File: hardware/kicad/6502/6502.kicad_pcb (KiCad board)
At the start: 2 copper layers, 35 parts, among them J1 Barrel_Jack, J2 Bus_Header, J3 VIA_Header, SW1 SW_Push, SW2 SW_Push, SW3 SW_Push, SW4 SW_Push, SW5 SW_Push, U1 L7805, U2 W65C02SxP, U3 28C256, U4 HM62256BLP, U5 W65C22SxP, U6 74LS00, U7 74LS00, X1 CXO_DIP8, X1 TFT680

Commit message: End of day 8/24.
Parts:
- removed the X1 at (179.1, 90.2)
- added G***: LOGO, Graphics:logo, F.Cu at (196.0, 119.0)
- added REF**: MountingHole_3.5mm, MountingHole:MountingHole_3.5mm, F.Cu at (63.5, 143.5)
- added REF**: MountingHole_3.5mm, MountingHole:MountingHole_3.5mm, F.Cu at (223.5, 143.5)
- added REF**: MountingHole_3.5mm, MountingHole:MountingHole_3.5mm, F.Cu at (63.0, 36.5)
- added REF**: MountingHole_3.5mm, MountingHole:MountingHole_3.5mm, F.Cu at (223.0, 37.5)
- R1, R2, R3, R4, R5, R6: footprint Resistor_THT:R_Axial_Power_L25.0mm_W9.0mm_P10.16mm_Vertical -> Resistor_THT:R_Axial_DIN0207_L6.3mm_D2.5mm_P10.16mm_Horizontal
- U1: footprint Package_TO_SOT_THT:TO-220-5_Horizontal_TabDown -> Package_TO_SOT_THT:TO-220-3_Horizontal_TabDown
- U3, U4: footprint Package_DIP:DIP-28_W15.24mm -> Package_DIP:DIP-28_W15.24mm_Socket
- U5: footprint Package_DIP:DIP-42_W15.24mm -> Package_DIP:DIP-40_W15.24mm_Socket
- moved C4 136.5 mm to (203.7, 46.8), turned to -90 degrees
- moved C6 132.0 mm to (214.6, 67.3)
- moved C5 128.7 mm to (203.7, 85.1), turned to -90 degrees
- moved U6 125.9 mm to (210.0, 72.3)
- moved U5 121.1 mm to (103.4, 87.5), turned to 90 degrees
- moved U7 105.6 mm to (210.0, 46.8)
- moved J1 95.5 mm to (86.7, 132.0)
- moved C1 90.2 mm to (73.8, 105.2), turned to 90 degrees
- moved J3 89.0 mm to (164.3, 97.6), turned to 90 degrees
- moved RV1 79.2 mm to (211.5, 96.5)
- moved D2 77.2 mm to (87.2, 103.2), turned to -90 degrees
- moved J2 70.7 mm to (151.9, 96.4), turned to -90 degrees
- moved R4 68.4 mm to (154.5, 120.0)
- moved U4 65.9 mm to (196.1, 72.2), turned to -90 degrees
- moved R5 65.7 mm to (154.5, 127.0)
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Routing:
- net VCC: track 0.00 -> 620.3 mm
- net /~{RW}: track 0.00 -> 106.2 mm
- net /PHI1: track 0.00 -> 70.7 mm
- net Net-(C1-Pad1): track 0.00 -> 32.5 mm
- net Net-(U7-Pad11): track 0.00 -> 20.4 mm
- net /A14: track 0.00 -> 17.2 mm
- net Net-(U7-Pad12): track 0.00 -> 12.7 mm
- net /A15: track 0.00 -> 11.3 mm
- net /~{PHI2}: track 0.00 -> 10.8 mm
- net /~{A15}: track 0.00 -> 9.72 mm
- net Net-(D1-Pad2): track 0.00 -> 8.50 mm
- net /PHI2: track 0.00 -> 6.13 mm
- net Net-(D2-Pad1): track 0.00 -> 5.90 mm
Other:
- board outline added: 172 x 116 mm
- board text added: "+5V"
- board text added: "-Connect RDY to VCC W/O Graphics Card -Connect PHI1 to PHI2 W/O External Clock"
- board text added: "0.1µF"
- board text added: "1K"
- board text added: "1N5819"
- board text added: "1µF"
- board text added: "6502 Prototype Korey Bliss (https://github.com/kblissExternal/6502)"
- board text added: "74LS00"
- board text added: "A0"
- board text added: "A1"
- board text added: "A10"
- board text added: "A11"
- board text added: "A12"
- board text added: "A13"
- board text added: "A14"
- board text added: "A15"
- board text added: "A2"
- board text added: "A3"
- board text added: "A4"
- board text added: "A5"
- board text added: "A6"
- board text added: "A7"
- board text added: "A8"
- board text added: "A9"
- board text added: "AS6C62256"
- board text added: "AT28C256"
- board text added: "CB1"
- board text added: "CB2"
- board text added: "CLOCK"
- board text added: "CNTRST"
- board text added: "CONTRAST"
- board text added: "D0"
- board text added: "D1"
- board text added: "D2"
- board text added: "D3"
- board text added: "D4"
- board text added: "D5"
- board text added: "D6"
- board text added: "DOWN"
- board text added: "E7"
- board text added: "GND"
- board text added: "IRQ"
- board text added: "LEFT"
- board text added: "PA5"
- board text added: "PA6"
- board text added: "PA7"
- board text added: "PB0"
- board text added: "PB1"
- board text added: "PB2"
- board text added: "PB3"
- board text added: "PB4"
- board text added: "PB5"
- board text added: "PB6"
- board text added: "PB7"
- board text added: "PHI1"
- board text added: "PHI2"
- board text added: "POWER"
- board text added: "RDY"
- board text added: "RESET"
- board text added: "RIGHT"
- board text added: "RW"
- board text added: "Revision 1.0 (8/24/22)"
- board text added: "UP"
- board text added: "VCC"
- board text added: "W65C22S"
- board text added: "WDC65C02"

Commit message: Added final hardware files for revision 1.0.
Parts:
- moved NW 1.60 mm to (63.0, 38.1)
- renumbered REF** to NE, REF** to NW, REF** to SE, REF** to SW
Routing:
- net GND: track 0.00 -> 469.6 mm
- net /A14: track 17.2 -> 224.8 mm, vias 0 -> 1
- net /PHI2: track 6.13 -> 195.0 mm
- net /RDY: track 0.00 -> 171.6 mm
- net /D0: track 0.00 -> 170.0 mm, vias 0 -> 1
- net /A15: track 11.3 -> 180.3 mm
- net /A12: track 0.00 -> 167.4 mm
- net /A1: track 0.00 -> 166.4 mm, vias 0 -> 1
- net /A13: track 0.00 -> 163.2 mm
- net /A8: track 0.00 -> 150.7 mm, vias 0 -> 2
- net /D1: track 0.00 -> 149.9 mm, vias 0 -> 1
- net /A3: track 0.00 -> 146.8 mm, vias 0 -> 2
- net /D7: track 0.00 -> 142.6 mm, vias 0 -> 2
- net /~{PHI2}: track 10.8 -> 151.5 mm, vias 0 -> 1
- net /D6: track 0.00 -> 137.8 mm, vias 0 -> 2
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
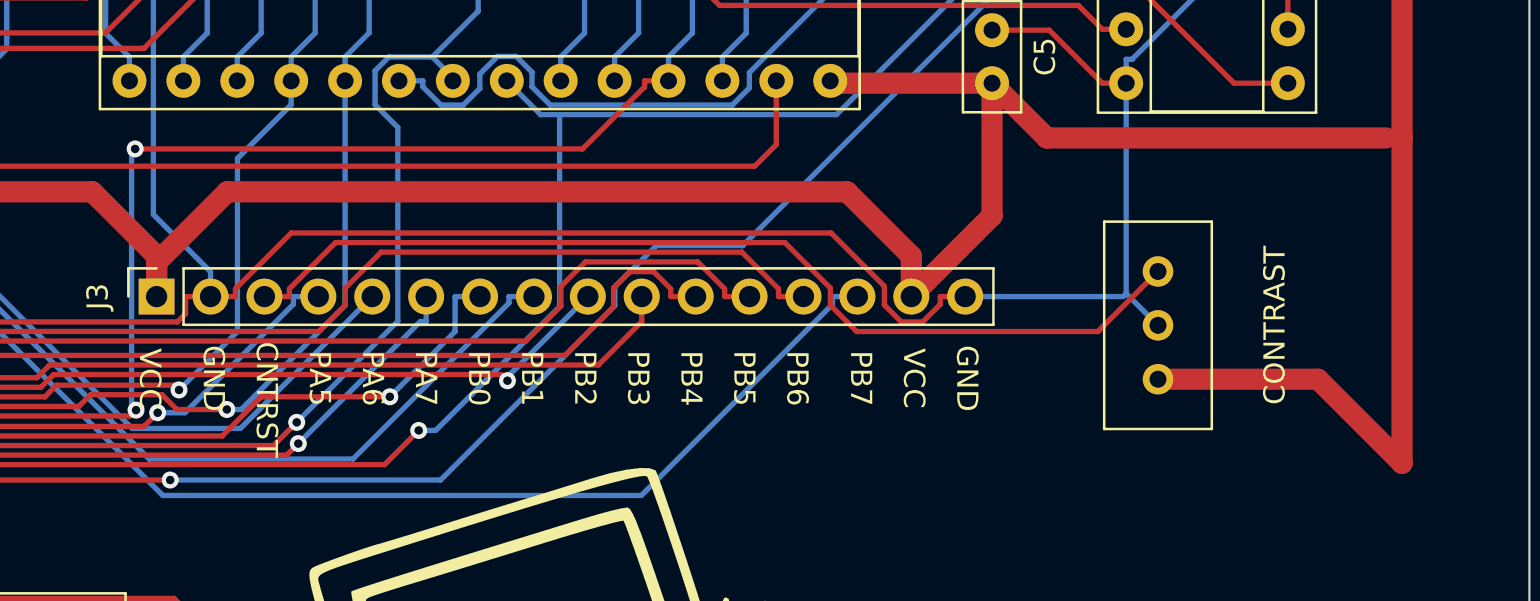
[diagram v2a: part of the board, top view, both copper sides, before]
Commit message: Corrected some minor rev 1.0 issues.
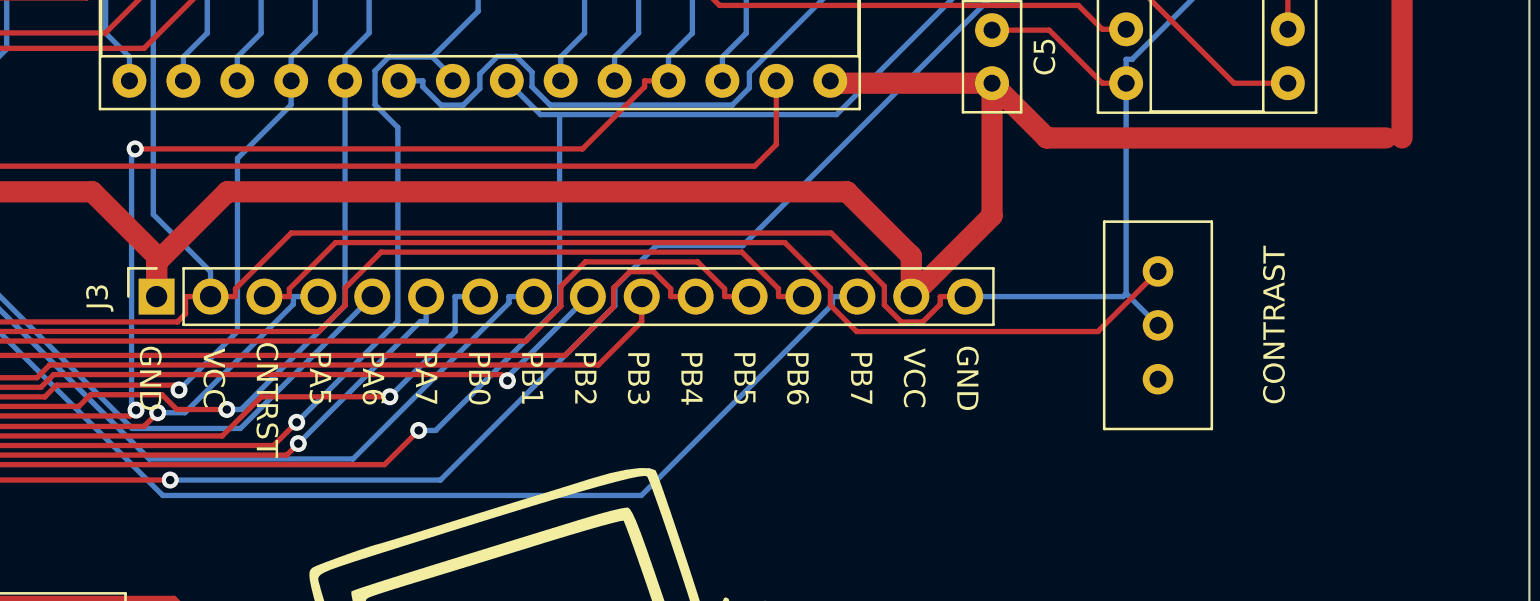
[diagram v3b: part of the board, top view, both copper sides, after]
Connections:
- J3 pad 1: VCC -> GND
- J3 pad 2: GND -> VCC
- RV1 pad 3: VCC -> unconnected-(RV1-Pad3)
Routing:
- net VCC: track 679.1 -> 650.6 mm
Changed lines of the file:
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@@
   (net 74 "Net-(U7-Pad12)")
   (net 75 "/~{PHI2}")
+  (net 76 "unconnected-(RV1-Pad3)")
   (footprint "Capacitor_THT:C_Radial_D4.0mm_H5.0mm_P1.50mm" (layer "F.Cu")
     (at 73.825 105.25 90)
@@
       (net 2 "GND") (pinfunction "2") (pintype "passive"))
     (pad "3" thru_hole circle (at 0 5.08) (size 1.44 1.44) (drill 0.8) (layers *.Cu *.Mask)
-      (net 3 "VCC") (pinfunction "3") (pintype "passive"))
+      (net 76 "unconnected-(RV1-Pad3)") (pinfunction "3") (pintype "passive+no_connect"))
     (model "${KICAD6_3DMODEL_DIR}/Potentiometer_THT.3dshapes/Potentiometer_Bourns_3386C_Horizontal.wrl"
       (offset (xyz 0 0 0))
@@
     (fp_line (start 0.635 -1.27) (end 1.27 -0.635) (layer "F.Fab") (width 0.1))
     (pad "1" thru_hole rect (at 0 0 90) (size 1.7 1.7) (drill 1) (layers *.Cu *.Mask)
-      (net 3 "VCC") (pinfunction "Pin_1") (pintype "passive"))
+      (net 2 "GND") (pinfunction "Pin_1") (pintype "passive"))
     (pad "2" thru_hole oval (at 0 2.54 90) (size 1.7 1.7) (drill 1) (layers *.Cu *.Mask)
-      (net 2 "GND") (pinfunction "Pin_2") (pintype "passive"))
+      (net 3 "VCC") (pinfunction "Pin_2") (pintype "passive"))
     (pad "3" thru_hole oval (at 0 5.08 90) (size 1.7 1.7) (drill 1) (layers *.Cu *.Mask)
       (net 18 "/CNTRST") (pinfunction "Pin_3") (pintype "passive"))
@@
     (effects (font (size 1 1) (thickness 0.15)))
   )
-  (gr_text "GND" (at 167 101.5 270) (layer "F.SilkS")
+  (gr_text "VCC" (at 167 101.5 270) (layer "F.SilkS")
     (effects (font (size 1 1) (thickness 0.15)))
   )
@@
     (effects (font (size 1 1) (thickness 0.15)))
   )
-  (gr_text "VCC" (at 164 101.5 270) (layer "F.SilkS")
+  (gr_text "GND" (at 164 101.5 270) (layer "F.SilkS")
     (effects (font (size 1 1) (thickness 0.15)))
   )
@@
   (segment (start 121.135 65.555) (end 121.135 62.085) (width 1) (layer "F.Cu") (net 3))
   (segment (start 203.68 93.84) (end 199.875 97.645) (width 1) (layer "F.Cu") (net 3))
-  (segment (start 223 105.5) (end 219.04 101.54) (width 1) (layer "F.Cu") (net 3))
   (segment (start 199.39 40.2165) (end 199.39 40.64) (width 0.25) (layer "F.Cu") (net 3))
   (segment (start 199.39 45.05) (end 199.39 40.64) (width 1) (layer "F.Cu") (net 3))
@@
   (segment (start 92.03 80.01) (end 74.0046 80.01) (width 1) (layer "F.Cu") (net 3))
   (segment (start 69 70.27) (end 69 83.4) (width 1) (layer "F.Cu") (net 3))
-  (segment (start 219.04 101.54) (end 211.5 101.54) (width 1) (layer "F.Cu") (net 3))
   (segment (start 73.77 117.54) (end 73.77 119.27) (width 1) (layer "F.Cu") (net 3))
   (segment (start 74.0046 79.9754) (end 74.0046 80.01) (width 0.25) (layer "F.Cu") (net 3))
@@
   (segment (start 164.315 97.645) (end 164.315 96.035) (width 1) (layer "F.Cu") (net 3))
   (segment (start 151.615 87.485) (end 151.615 88.785) (width 1) (layer "F.Cu") (net 3))
-  (segment (start 223 90.17) (end 223 105.5) (width 1) (layer "F.Cu") (net 3))
   (segment (start 69.49 69.78) (end 73.75 69.78) (width 1) (layer "F.Cu") (net 3))
   (segment (start 151.88 97.5453) (end 152.1873 97.5453) (width 0.25) (layer "B.Cu") (net 3))

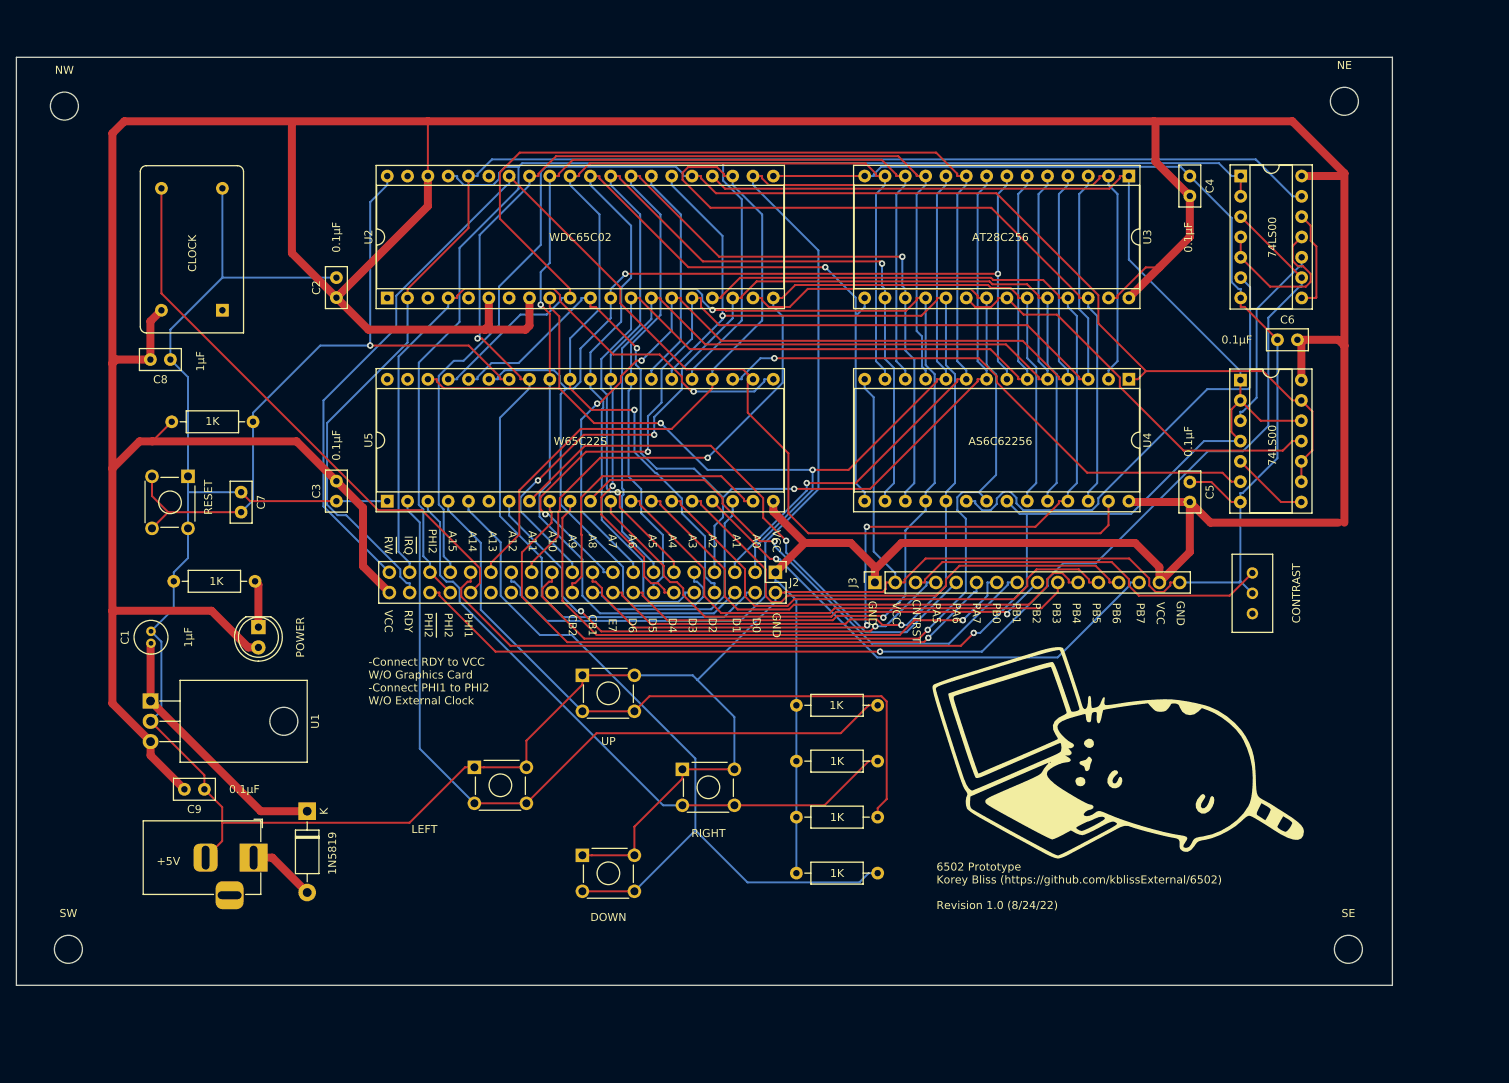
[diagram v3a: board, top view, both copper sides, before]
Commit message: Update to Revision 1.1 (primarily adding 6551).
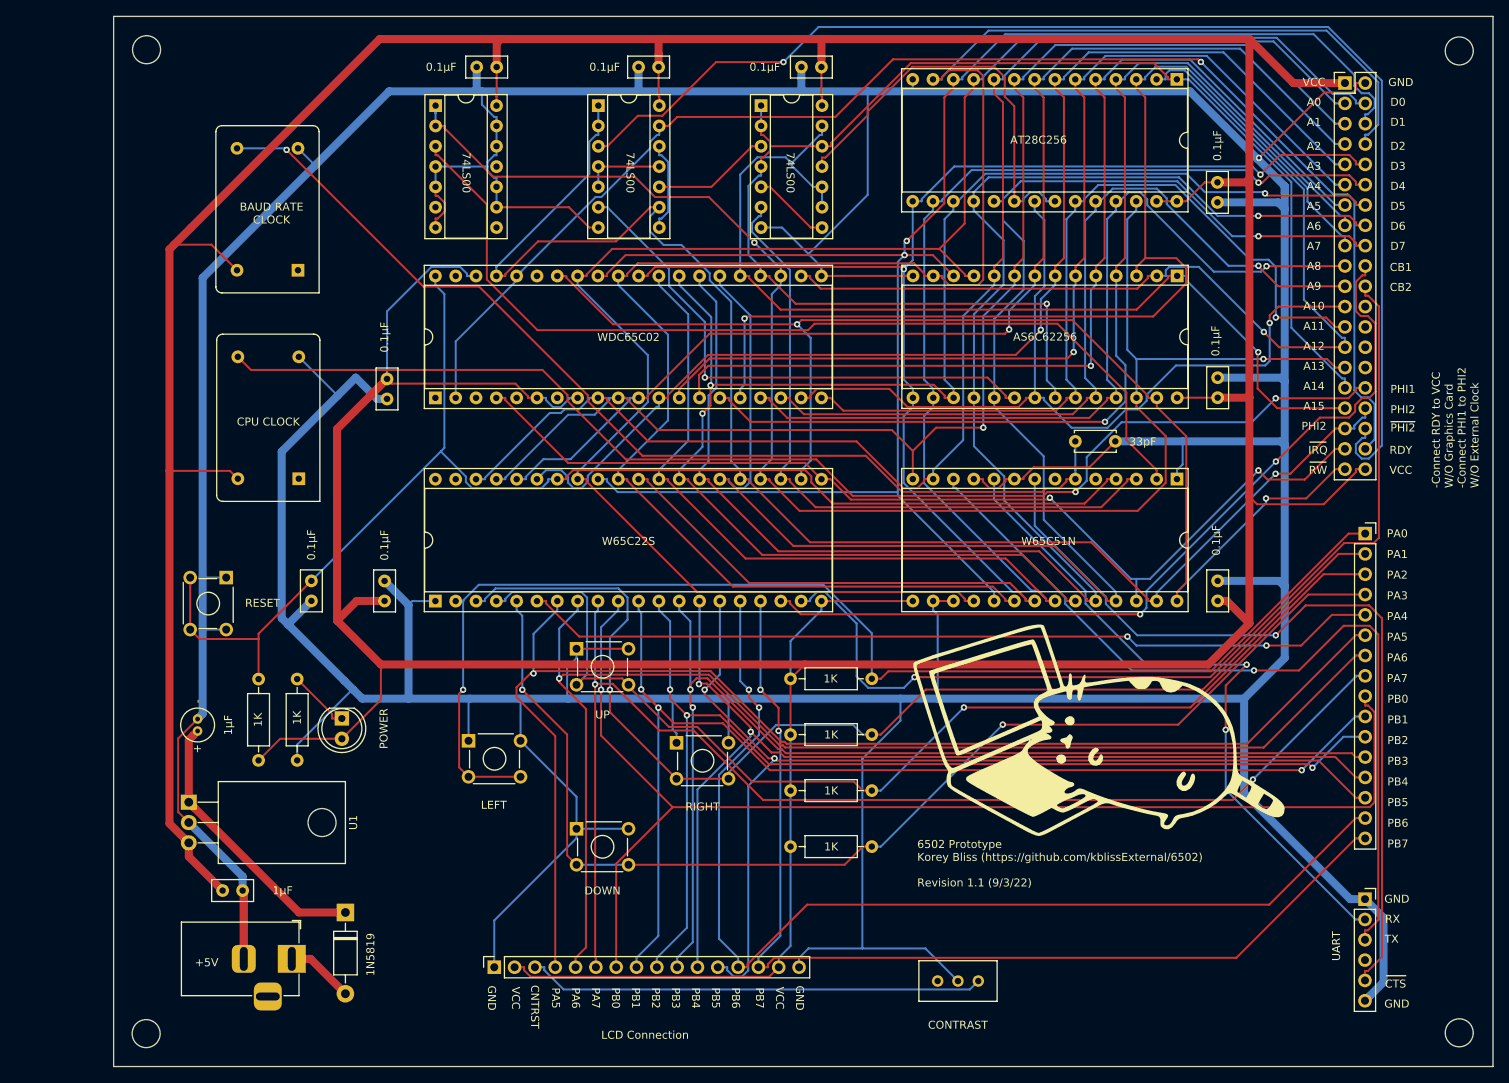
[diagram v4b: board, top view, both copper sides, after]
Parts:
- added C10: 33pF, Capacitor_THT:C_Disc_D5.0mm_W2.5mm_P5.00mm, F.Cu at (189.4, 80.0)
- added C11: 0.1µF, Capacitor_THT:C_Disc_D5.0mm_W2.5mm_P2.50mm, F.Cu at (155.1, 33.2)
- added C12: 0.1µF, Capacitor_THT:C_Disc_D5.0mm_W2.5mm_P2.50mm, F.Cu at (207.1, 50.1)
- added J4: UART_Header, Connector_PinSocket_2.54mm:PinSocket_1x06_P2.54mm_Vertical, F.Cu at (225.6, 137.2)
- added J5: VIA_Header, Connector_PinSocket_2.54mm:PinSocket_1x16_P2.54mm_Vertical, F.Cu at (225.6, 91.5)
- added U8: W65C51NxP, Package_DIP:DIP-28_W15.24mm_Socket, F.Cu at (202.1, 84.7)
- added U9: 74LS00, Package_DIP:DIP-14_W7.62mm_Socket, F.Cu at (109.4, 38.0)
- added X2: TFT680, Oscillator:Oscillator_DIP-14, F.Cu at (92.2, 58.6)
- J3: value VIA_Header -> LCD_Header
- moved J2 93.8 mm to (223.1, 35.2), turned to 0 degrees
- moved C6 86.8 mm to (134.8, 33.2)
- moved U7 80.8 mm to (129.7, 38.0)
- moved U6 69.0 mm to (150.1, 38.0)
- moved J3 67.7 mm to (116.7, 145.7)
- moved RV1 61.4 mm to (177.2, 147.5), turned to -90 degrees
- moved C8 52.9 mm to (114.5, 33.2), turned to 0 degrees
- moved R2 43.7 mm to (87.3, 119.9), turned to 90 degrees
- moved C4 25.4 mm to (207.2, 72.0)
- moved X1 23.1 mm to (92.3, 84.7)
- moved SE 17.3 mm to (237.4, 153.9)
- moved C7 16.2 mm to (93.9, 99.9), turned to 90 degrees
- moved NE 15.7 mm to (237.4, 31.2)
- moved D2 15.5 mm to (97.7, 114.6)
- moved SW 14.3 mm to (73.2, 154.0)
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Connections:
- U7 pad 9: /~{PHI2} -> /PHI2
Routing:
- net GND: track 469.6 -> 921.7 mm, vias 0 -> 1
- net /PHI3: track 0.00 -> 128.6 mm, vias 0 -> 1
- net /~{ACIACS}: track 0.00 -> 118.3 mm
- net /PA4: track 0.00 -> 107.6 mm, vias 0 -> 2
- net /UART_RX: track 0.00 -> 106.0 mm, vias 0 -> 1
- net /~{UART_RTS}: track 0.00 -> 104.0 mm, vias 0 -> 1
- net /D2: track 133.3 -> 237.1 mm, vias 1 -> 0
- net /PA5: track 65.9 -> 163.6 mm, vias 2 -> 1
- net /PA6: track 70.8 -> 158.1 mm
- net /PHI1: track 70.7 -> 156.1 mm, vias 0 -> 2
- net /CB2: track 36.7 -> 121.8 mm, vias 0 -> 1
- net /UART_TX: track 0.00 -> 84.4 mm, vias 0 -> 2
- net /PB0: track 72.6 -> 155.2 mm
- net VCC: track 650.6 -> 732.7 mm
- net /PA7: track 76.5 -> 154.7 mm, vias 1 -> 2
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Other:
- board size 172 x 116 mm -> 172.4 x 131.3 mm
- board text added: "+"
- board text added: "-"
- board text added: "33pF"
- board text added: "BAUD RATE CLOCK"
- board text added: "CPU CLOCK"
- board text added: "CTS"
- board text added: "D7"
- board text added: "LCD Connection"
- board text added: "PA0"
- board text added: "PA1"
- board text added: "PA2"
- board text added: "PA3"
- board text added: "PA4"
- board text added: "RX"
- board text added: "Revision 1.1 (9/3/22)"
- board text added: "TX"
- board text added: "UART"
- board text added: "W65C51N"
- board text removed: "CLOCK"
- board text removed: "E7"
- board text removed: "Revision 1.0 (8/24/22)"
